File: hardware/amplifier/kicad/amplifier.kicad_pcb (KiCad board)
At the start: 2 copper layers, 35.6 x 26.2 mm, 16 parts, among them J1 SMA-J-P-H-ST-TH1, J2 SMA-J-P-H-ST-TH1, J3 Conn_01x04, J4 Conn_01x04, U1 TSY-83LN+

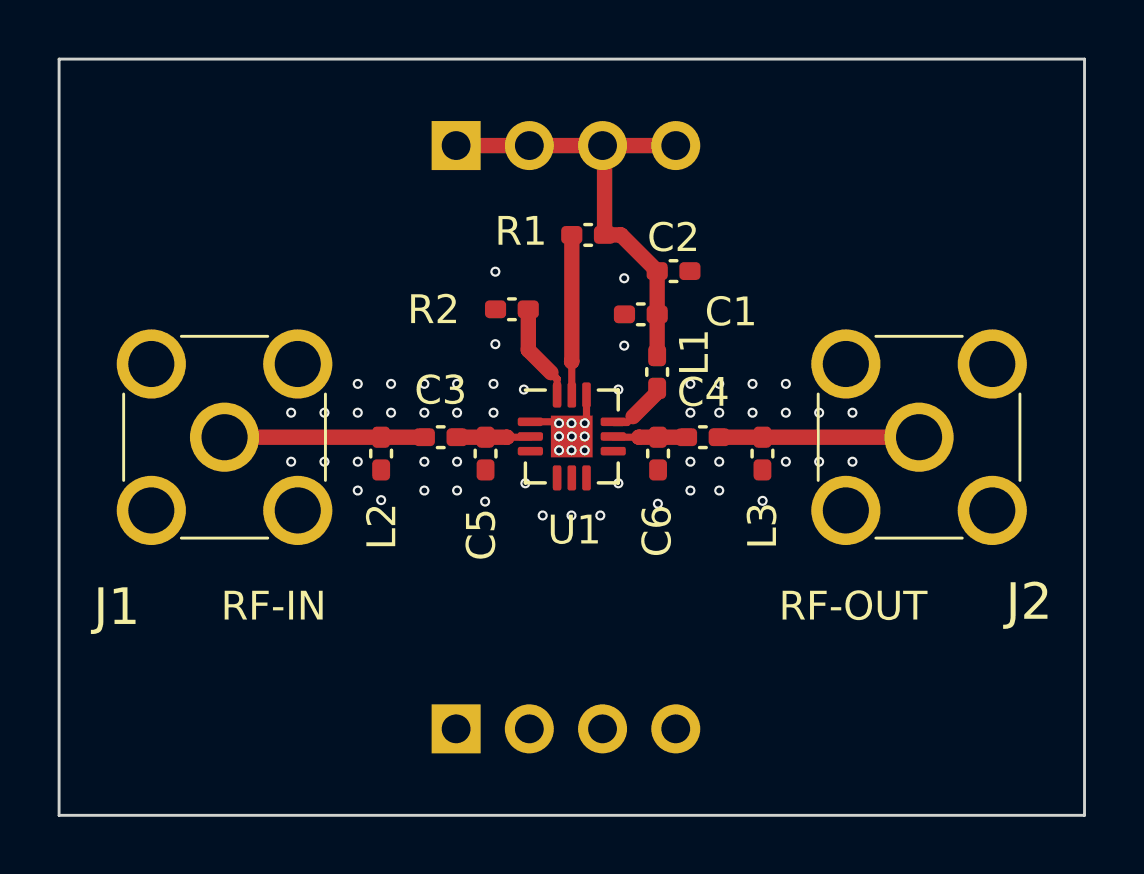
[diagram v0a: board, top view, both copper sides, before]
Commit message: Change layout for amplifier for DIY production
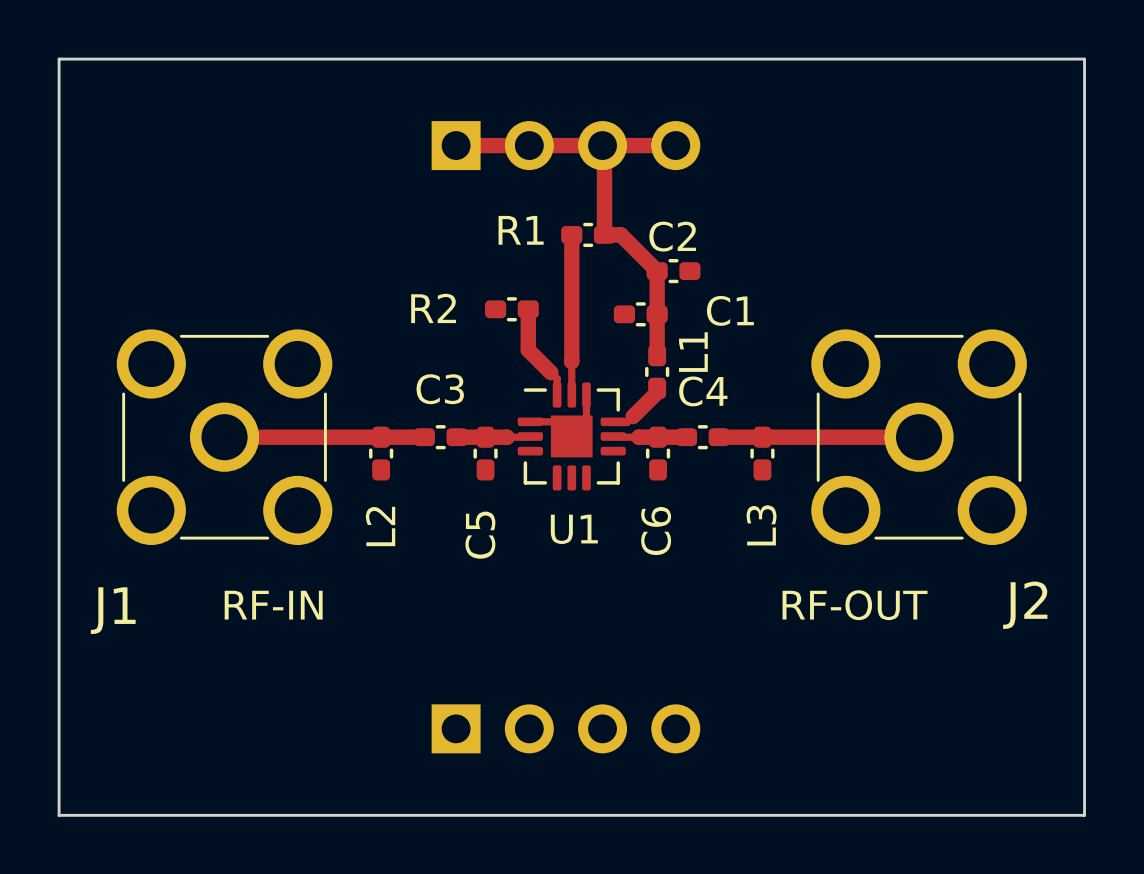
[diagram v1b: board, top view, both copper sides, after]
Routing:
- net GND: vias 61 -> 0
